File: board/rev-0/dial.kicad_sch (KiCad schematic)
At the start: 46 parts, among them U2 SN74LV1T34DBV, U3 APDS-9306-065, U4 MT6701CT, U5 NAU7802SGI, U6 TMC6300-LA-T

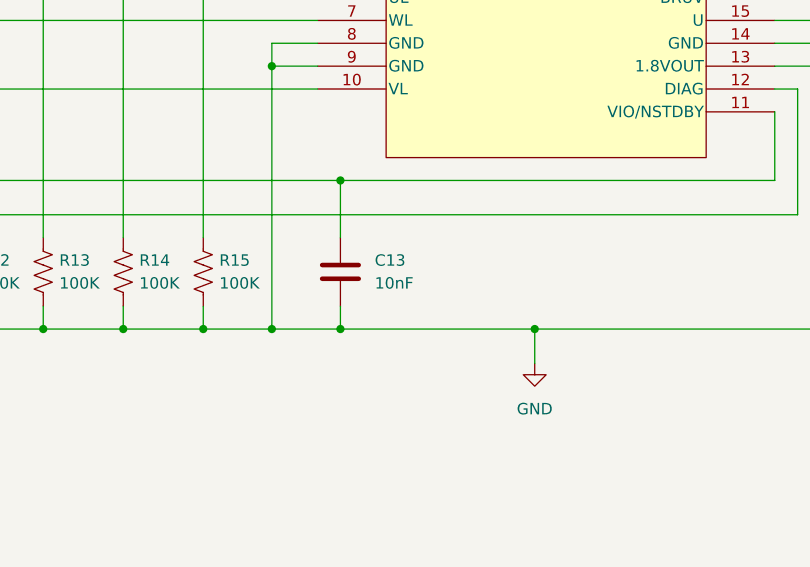
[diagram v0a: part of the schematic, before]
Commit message: Updated TMC6300 VIO cap to 100nF
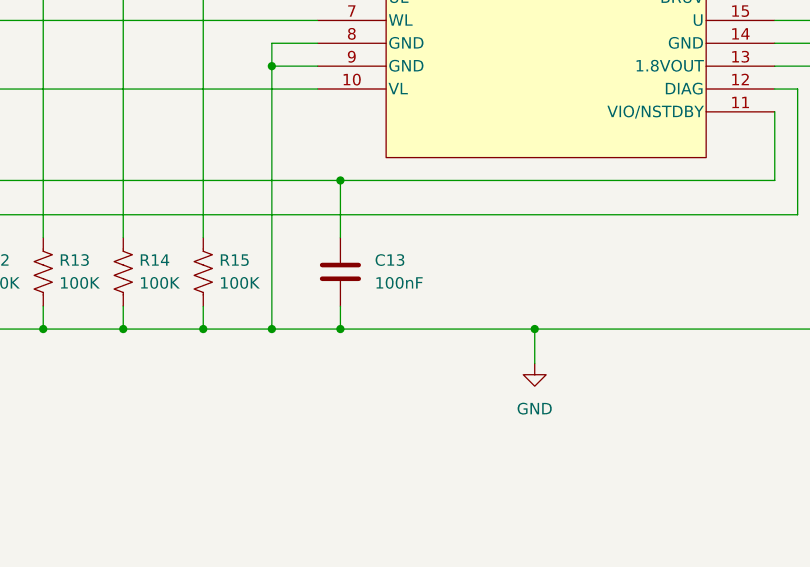
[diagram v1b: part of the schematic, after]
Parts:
- C13: value 10nF -> 100nF
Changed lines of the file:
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@@
 			)
 		)
-		(property "Value" "10nF"
+		(property "Value" "100nF"
 			(at 354.33 157.4799 0)
 			(effects

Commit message: Added key LEDs
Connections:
- net LED_DATA renamed DIAL_LED_DATA
- net LED_DATA_5V renamed DIAL_LED_DATA_5V
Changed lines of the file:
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@@
 		)
 	)
-	(label "LED_DATA_5V"
+	(label "DIAL_LED_DATA_5V"
 		(at 91.44 334.01 0)
 		(effects
@@
 		)
 	)
-	(global_label "LED_DATA"
+	(global_label "DIAL_LED_DATA"
 		(shape input)
 		(at 50.8 334.01 180)
@@
 		)
 		(property "Intersheetrefs" "${INTERSHEET_REFS}"
-			(at 38.9853 334.01 0)
+			(at 34.0262 334.01 0)
 			(effects
 				(font

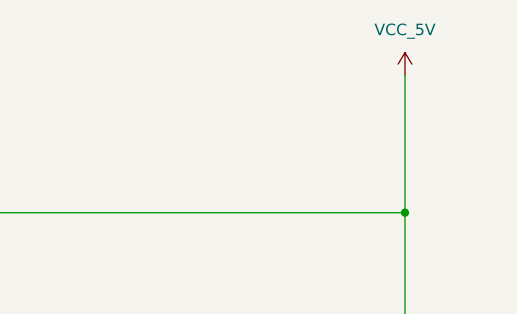
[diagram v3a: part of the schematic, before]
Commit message: Added power circuitry
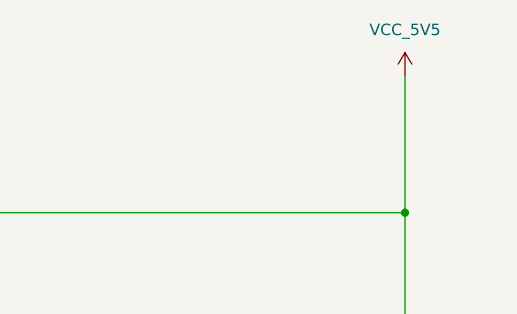
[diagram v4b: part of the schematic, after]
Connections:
- net VCC_5V renamed VCC_5V5
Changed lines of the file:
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@@
 	(title_block
 		(title "Dial")
-		(date "2025-03-28")
+		(date "2025-04-20")
 		(rev "0")
 		(company "Biro")
@@
 	)
 	(bus_alias "MTR_OUT"
-		(members "SDA" "SCL")
+		(members "U" "V" "W")
 	)
 	(junction
@@
 			)
 		)
-		(property "Value" "VCC_5V"
+		(property "Value" "VCC_5V5"
 			(at 508 71.12 0)
 			(effects
@@
 			)
 		)
-		(property "Description" "Power symbol creates a global label with name \"VCC_5V\""
+		(property "Description" "Power symbol creates a global label with name \"VCC_5V5\""
 			(at 508 76.2 0)
 			(effects

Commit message: First crack at layout, added scottokeebs 3d files
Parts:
- C10, C11, C12, C13, C14, C15, C16, C17, C18, C19, C20, C21, C22, C3, C4, C5, C6, C7, C8, C9: footprint (none) -> Capacitor_SMD:C_0603_1608Metric
- R10, R11, R12, R13, R14, R15, R8, R9: footprint (none) -> Resistor_SMD:R_0603_1608Metric
- R4, R5, R6, R7: footprint (none) -> Resistor_SMD:R_2512_6332Metric
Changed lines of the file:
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@@
 			)
 		)
-		(property "Footprint" ""
+		(property "Footprint" "Resistor_SMD:R_0603_1608Metric"
 			(at 318.516 156.464 90)
 			(effects
@@
 			)
 		)
-		(property "Footprint" ""
+		(property "Footprint" "Capacitor_SMD:C_0603_1608Metric"
 			(at 304.4952 246.38 0)
 			(effects
@@
 			)
 		)
-		(property "Footprint" ""
+		(property "Footprint" "Resistor_SMD:R_0603_1608Metric"
 			(at 300.736 156.464 90)
 			(effects
@@
 			)
 		)
-		(property "Footprint" ""
+		(property "Footprint" "Resistor_SMD:R_2512_6332Metric"
 			(at 284.226 245.364 90)
 			(effects
@@
 			)
 		)
-		(property "Footprint" ""
+		(property "Footprint" "Capacitor_SMD:C_0603_1608Metric"
 			(at 356.5652 332.74 0)
 			(effects
@@
 			)
 		)
-		(property "Footprint" ""
+		(property "Footprint" "Capacitor_SMD:C_0603_1608Metric"
 			(at 127.9652 128.27 0)
 			(effects
@@
 			)
 		)
-		(property "Footprint" ""
+		(property "Footprint" "Resistor_SMD:R_2512_6332Metric"
 			(at 284.226 232.664 90)
 			(effects
@@
 			)
 		)
-		(property "Footprint" ""
+		(property "Footprint" "Capacitor_SMD:C_0603_1608Metric"
 			(at 305.7652 332.74 0)
 			(effects
@@
 			)
 		)
-		(property "Footprint" ""
+		(property "Footprint" "Resistor_SMD:R_0603_1608Metric"
 			(at 294.894 256.794 90)
 			(effects
@@
 			)
 		)
-		(property "Footprint" ""
+		(property "Footprint" "Capacitor_SMD:C_0603_1608Metric"
 			(at 458.1652 332.74 0)
 			(effects
@@
 			)
 		)
-		(property "Footprint" ""
+		(property "Footprint" "Resistor_SMD:R_0603_1608Metric"
 			(at 309.626 156.464 90)
 			(effects
@@
 			)
 		)
-		(property "Footprint" ""
+		(property "Footprint" "Capacitor_SMD:C_0603_1608Metric"
 			(at 423.8752 101.6 0)
 			(effects
@@
 			)
 		)
-		(property "Footprint" ""
+		(property "Footprint" "Capacitor_SMD:C_0603_1608Metric"
 			(at 204.1652 332.74 0)
 			(effects
@@
 			)
 		)
-		(property "Footprint" ""
+		(property "Footprint" "Capacitor_SMD:C_0603_1608Metric"
 			(at 317.1952 227.33 0)
 			(effects
@@
 			)
 		)
-		(property "Footprint" ""
+		(property "Footprint" "Capacitor_SMD:C_0603_1608Metric"
 			(at 331.47 249.2248 0)
 			(effects
@@
 			)
 		)
-		(property "Footprint" ""
+		(property "Footprint" "Resistor_SMD:R_2512_6332Metric"
 			(at 271.526 245.364 90)
 			(effects
@@
 			)
 		)
-		(property "Footprint" ""
+		(property "Footprint" "Capacitor_SMD:C_0603_1608Metric"
 			(at 421.9448 138.43 0)
 			(effects
@@
 			)
 		)
-		(property "Footprint" ""
+		(property "Footprint" "Capacitor_SMD:C_0603_1608Metric"
 			(at 508.9652 332.74 0)
 			(effects
@@
 			)
 		)
-		(property "Footprint" ""
+		(property "Footprint" "Capacitor_SMD:C_0603_1608Metric"
 			(at 373.0752 227.33 0)
 			(effects
@@
 			)
 		)
-		(property "Footprint" ""
+		(property "Footprint" "Capacitor_SMD:C_0603_1608Metric"
 			(at 407.3652 332.74 0)
 			(effects
@@
 			)
 		)
-		(property "Footprint" ""
+		(property "Footprint" "Resistor_SMD:R_0603_1608Metric"
 			(at 327.406 156.464 90)
 			(effects
@@
 			)
 		)
-		(property "Footprint" ""
+		(property "Footprint" "Capacitor_SMD:C_0603_1608Metric"
 			(at 153.3652 332.74 0)
 			(effects
@@
 			)
 		)
-		(property "Footprint" ""
+		(property "Footprint" "Resistor_SMD:R_0603_1608Metric"
 			(at 336.296 156.464 90)
 			(effects
@@
 			)
 		)
-		(property "Footprint" ""
+		(property "Footprint" "Resistor_SMD:R_0603_1608Metric"
 			(at 294.894 237.744 90)
 			(effects
@@
 			)
 		)
-		(property "Footprint" ""
+		(property "Footprint" "Capacitor_SMD:C_0603_1608Metric"
 			(at 337.5152 262.89 0)
 			(effects
@@
 			)
 		)
-		(property "Footprint" ""
+		(property "Footprint" "Resistor_SMD:R_2512_6332Metric"
 			(at 271.526 232.664 90)
 			(effects
@@
 			)
 		)
-		(property "Footprint" ""
+		(property "Footprint" "Capacitor_SMD:C_0603_1608Metric"
 			(at 254.9652 332.74 0)
 			(effects
@@
 			)
 		)
-		(property "Footprint" ""
+		(property "Footprint" "Capacitor_SMD:C_0603_1608Metric"
 			(at 351.4852 160.02 0)
 			(effects
@@
 			)
 		)
-		(property "Footprint" ""
+		(property "Footprint" "Resistor_SMD:R_0603_1608Metric"
 			(at 291.846 156.464 90)
 			(effects
@@
 			)
 		)
-		(property "Footprint" ""
+		(property "Footprint" "Capacitor_SMD:C_0603_1608Metric"
 			(at 377.19 90.4748 0)
 			(effects
@@
 			)
 		)
-		(property "Footprint" ""
+		(property "Footprint" "Capacitor_SMD:C_0603_1608Metric"
 			(at 131.7752 246.38 0)
 			(effects
@@
 			)
 		)
-		(property "Footprint" ""
+		(property "Footprint" "Capacitor_SMD:C_0603_1608Metric"
 			(at 411.1752 101.6 0)
 			(effects

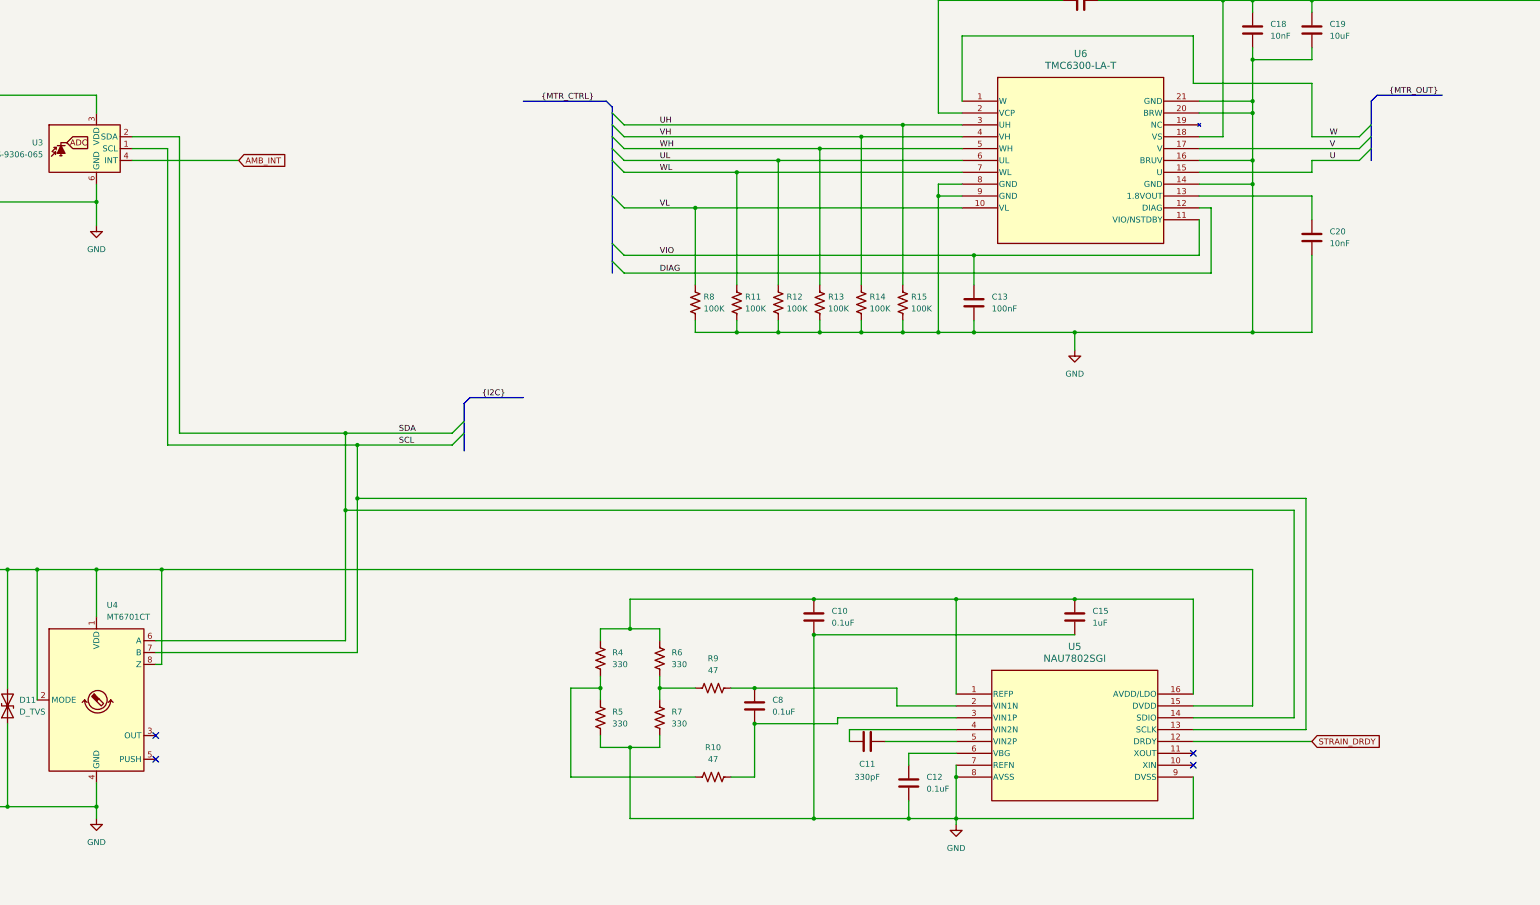
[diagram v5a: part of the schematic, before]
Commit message: Added battery divider to ADC, created board step file, updated to kicad 9
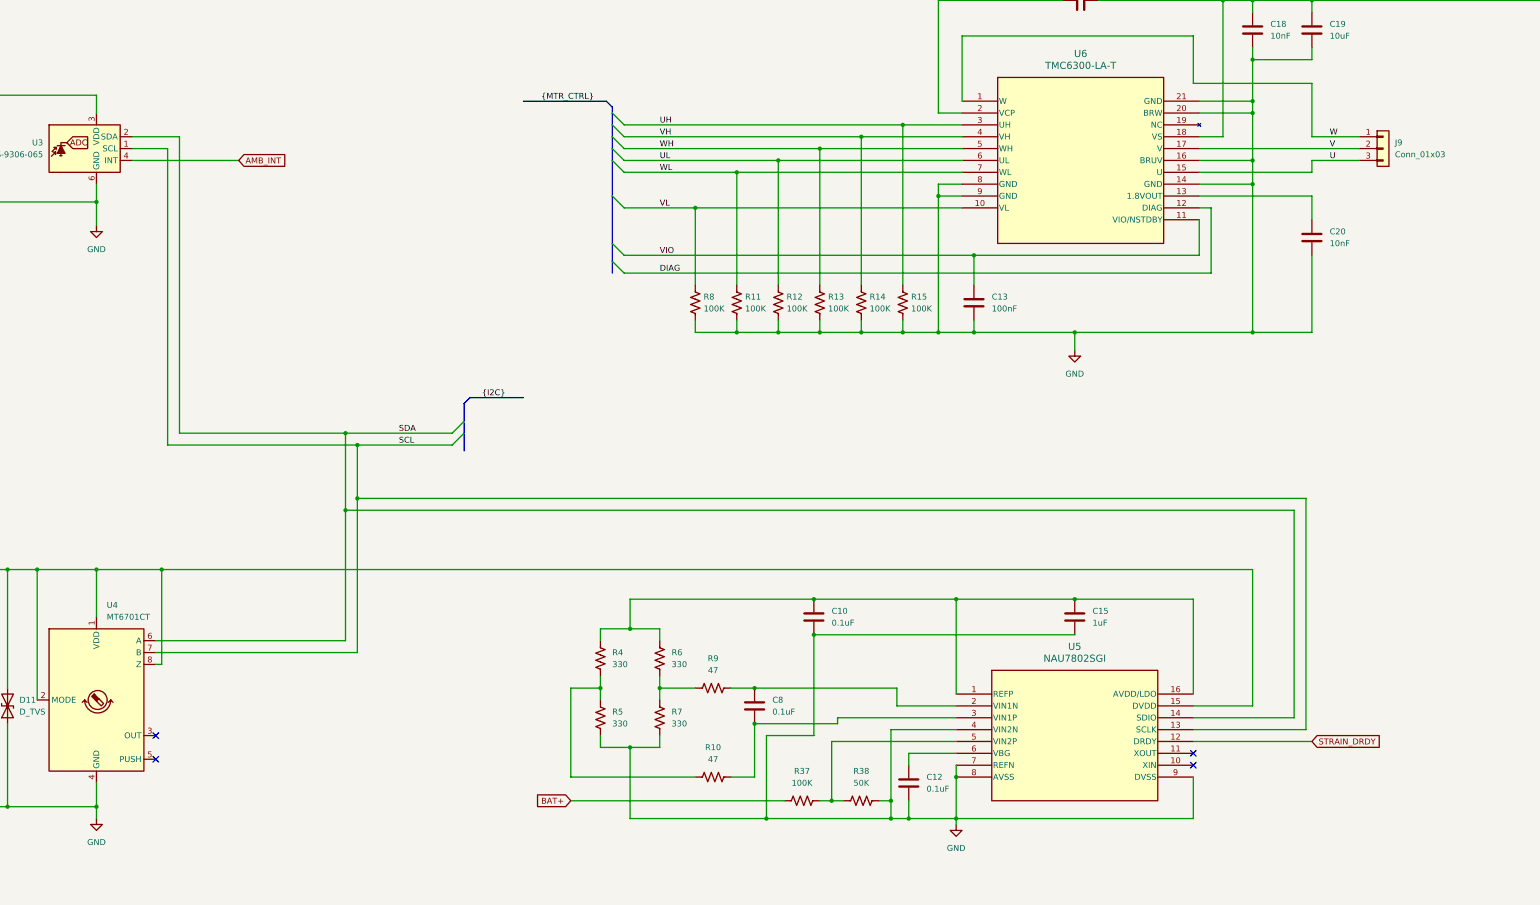
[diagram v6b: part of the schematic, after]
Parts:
- removed C11: 330pF, Capacitor_SMD:C_0603_1608Metric, symbol Device:C
- added J9: Conn_01x03, Connector_Wire:SolderWire-2sqmm_1x03_P7.8mm_D2mm_OD3.9mm, symbol Connector_Generic:Conn_01x03
- added R37: 100K, symbol Device:R_US
- added R38: 50K, symbol Device:R_US
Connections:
- net GND: now also U5.4 (VIN2N), R38.2
- net U: now also J9.3 (Pin_3)
- net V: now also J9.2 (Pin_2)
- net W: now also J9.1 (Pin_1)
- net at U5.5 (VIN2P): now also R37.2, R38.1
- new net BAT+: R37.1

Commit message: Added mounting holes, minor schematic fixes, layout progress
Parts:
- added C11: 0.1uF, Capacitor_SMD:C_0603_1608Metric, symbol Device:C
- R37, R38: footprint (none) -> Resistor_SMD:R_0603_1608Metric
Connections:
- net GND: now also C11.2
- net at R37.2, R38.1, U5.5 (VIN2P): now also C11.1
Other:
- moved on the sheet: C8, R37, R38
